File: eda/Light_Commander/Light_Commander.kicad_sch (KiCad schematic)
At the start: 12 parts, among them J1 GATE0, J10 BUFFB, J11 BUFFC, J12 BUFFD, J2 GATE1, J3 GATE2, J4 GATE3, J5 INA, J6 INB, J7 INC, J8 IND, J9 BUFFA

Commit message: Add OLED, LED strip connector, and LED level shifter to schematic
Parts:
- added J15: Conn_01x05, footprints:CUI_TBLH10V-350-05BK, symbol Connector_Generic:Conn_01x05
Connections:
- net GND: now also J15.2 (Pin_2), J15.5 (Pin_5)
- new net +5V_LED: J15.1 (Pin_1), J15.3 (Pin_3)
- new net LED_SPI: J15.4 (Pin_4)

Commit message: Add MDI in and thru to schematic
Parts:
- added J16: MIDI_IN, footprints:PJ301M-12_STEREO, symbol Connector_Audio:AudioJack2_Ground
- added J17: MIDI_THRU, footprints:PJ301M-12_STEREO, symbol Connector_Audio:AudioJack2_Ground
- added SW3, SW4: SW_DPDT_x2, footprints:CAS-220TA, symbol Switch:SW_DPDT_x2
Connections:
- net GND: now also J16.G, J17.G
- new net: J16.T, SW3.3 (C), SW3.4 (A)
- new net: J16.S, SW3.1 (A), SW3.6 (C)
- new net MIDI_IN_PIN_4: SW3.2 (B)
- new net MIDI_IN_PIN_5: SW3.5 (B)
- new net MIDI_THRU_PIN_4: SW4.2 (B)
- new net MIDI_THRU_PIN_5: SW4.5 (B)
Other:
- note added: "TRS MIDI A: Switch up as shown TRS MIDI B: Flipped down"

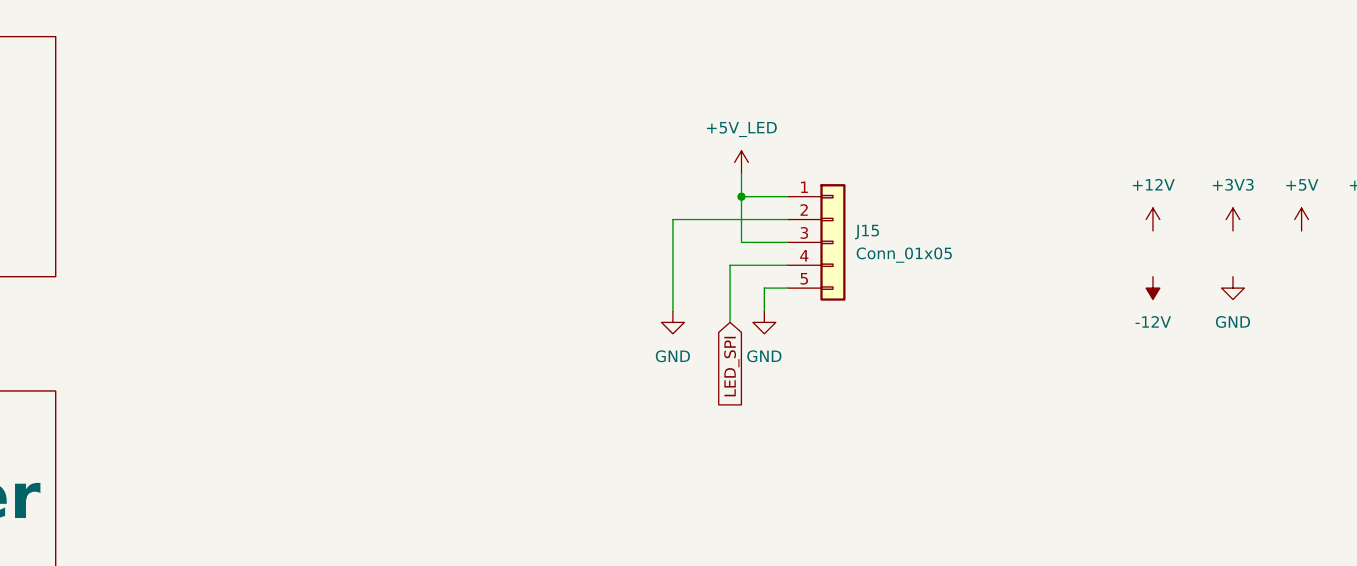
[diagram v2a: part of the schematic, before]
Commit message: Add buttons, SWD, and LED reverse polarity protection to schematic
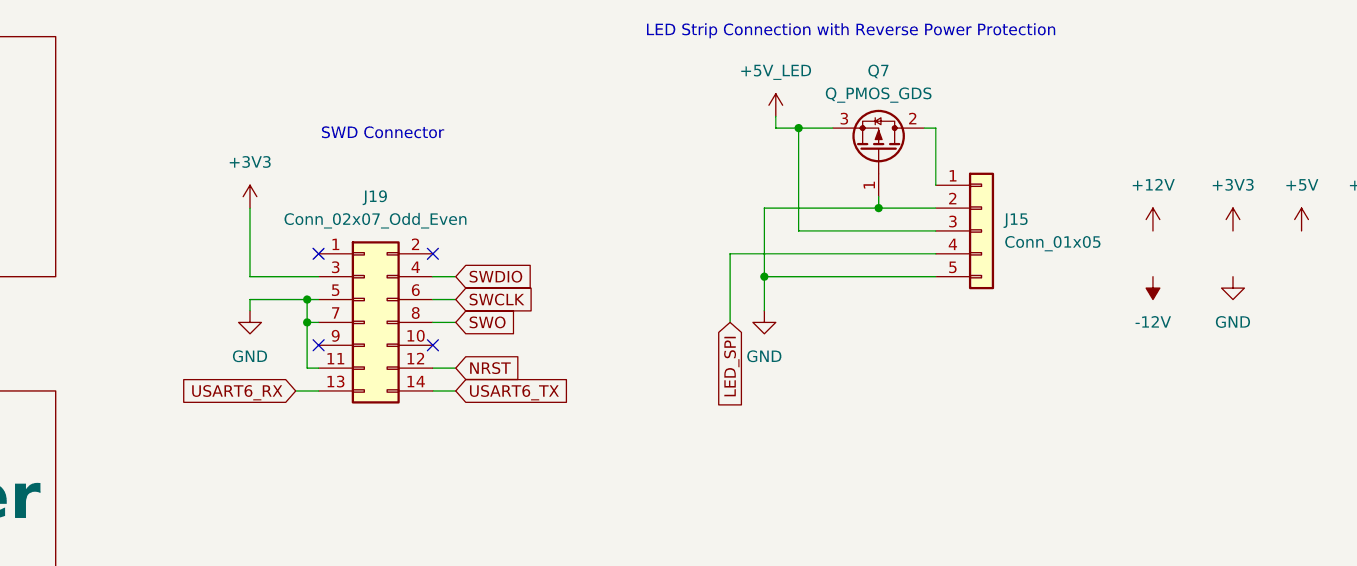
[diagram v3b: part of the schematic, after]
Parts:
- added J19: Conn_02x07_Odd_Even, symbol Connector_Generic:Conn_02x07_Odd_Even
- added Q7: Q_PMOS_GDS, Package_TO_SOT_SMD:TO-252-2, symbol Transistor_FET:Q_PMOS_GDS
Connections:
- net +3V3: now also J19.3 (Pin_3)
- net +5V_LED: now also Q7.3 (S); no longer J15.1 (Pin_1)
- net GND: now also J19.11 (Pin_11), J19.5 (Pin_5), J19.7 (Pin_7), Q7.1 (G)
- new net: J15.1 (Pin_1), Q7.2 (D)
- new net NRST: J19.12 (Pin_12)
- new net SWCLK: J19.6 (Pin_6)
- new net SWDIO: J19.4 (Pin_4)
- new net SWO: J19.8 (Pin_8)
- new net USART6_RX: J19.13 (Pin_13)
- new net USART6_TX: J19.14 (Pin_14)
- no-connect marks 4 -> 8
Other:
- note added: "LED Strip Connection with Reverse Power Protection"
- note added: "SWD Connector"
- moved on the sheet: J15

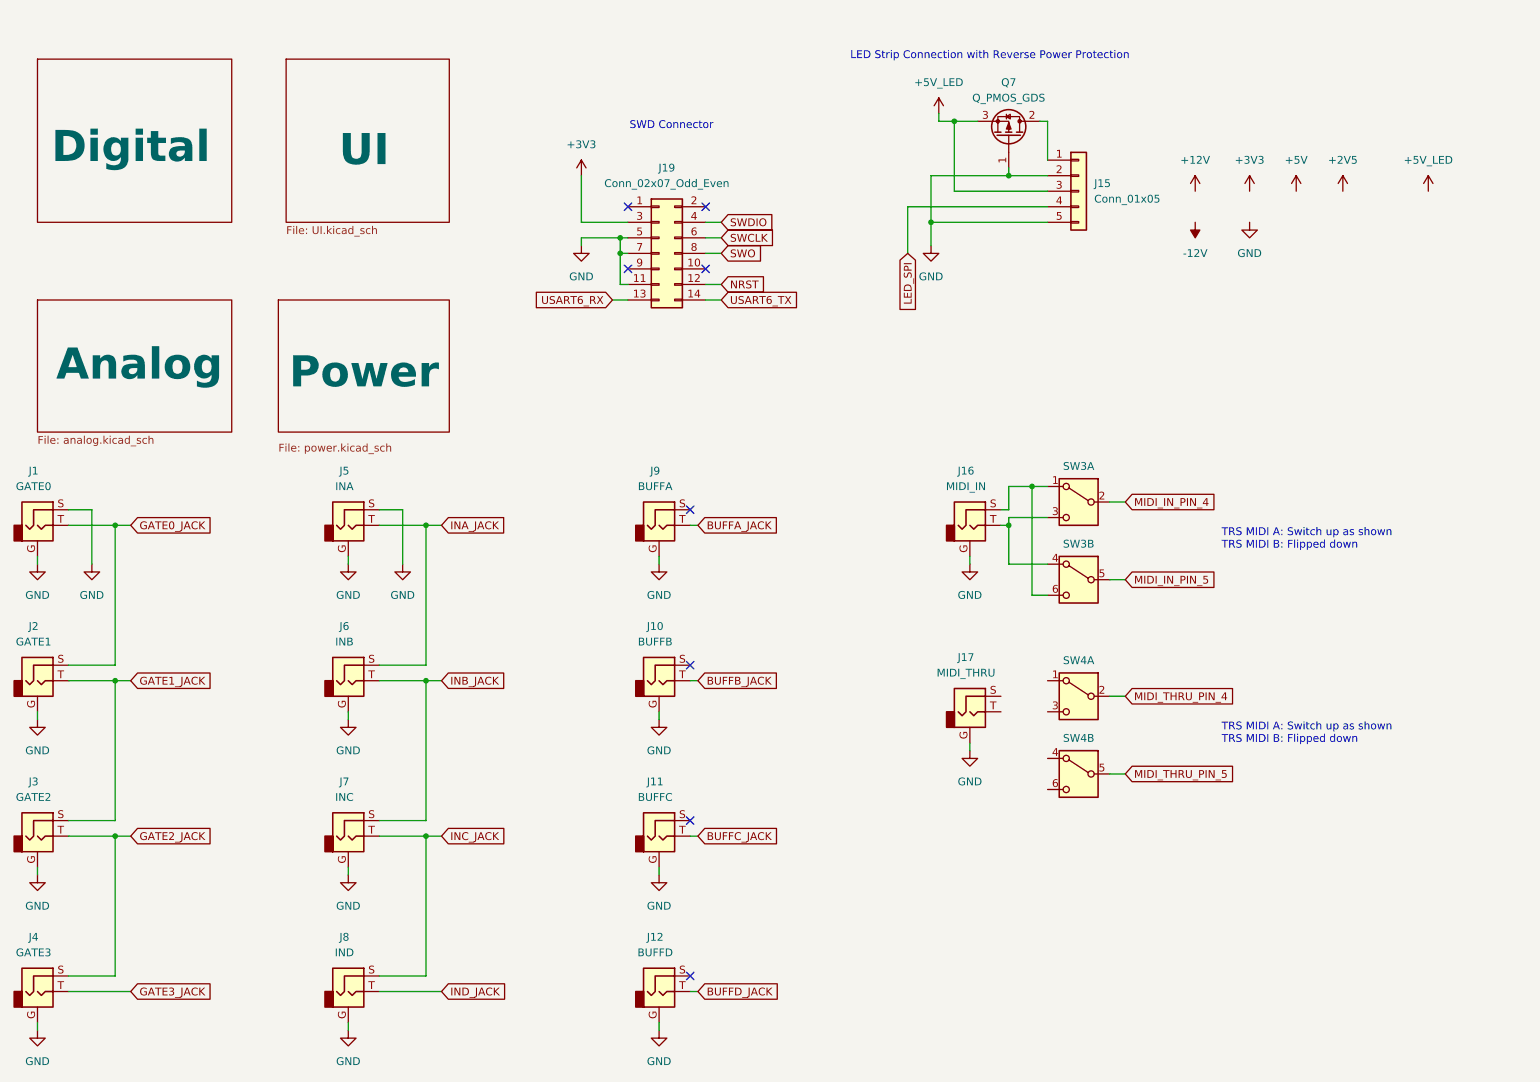
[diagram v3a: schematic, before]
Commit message: Fix footprints and finish first draft of schematic
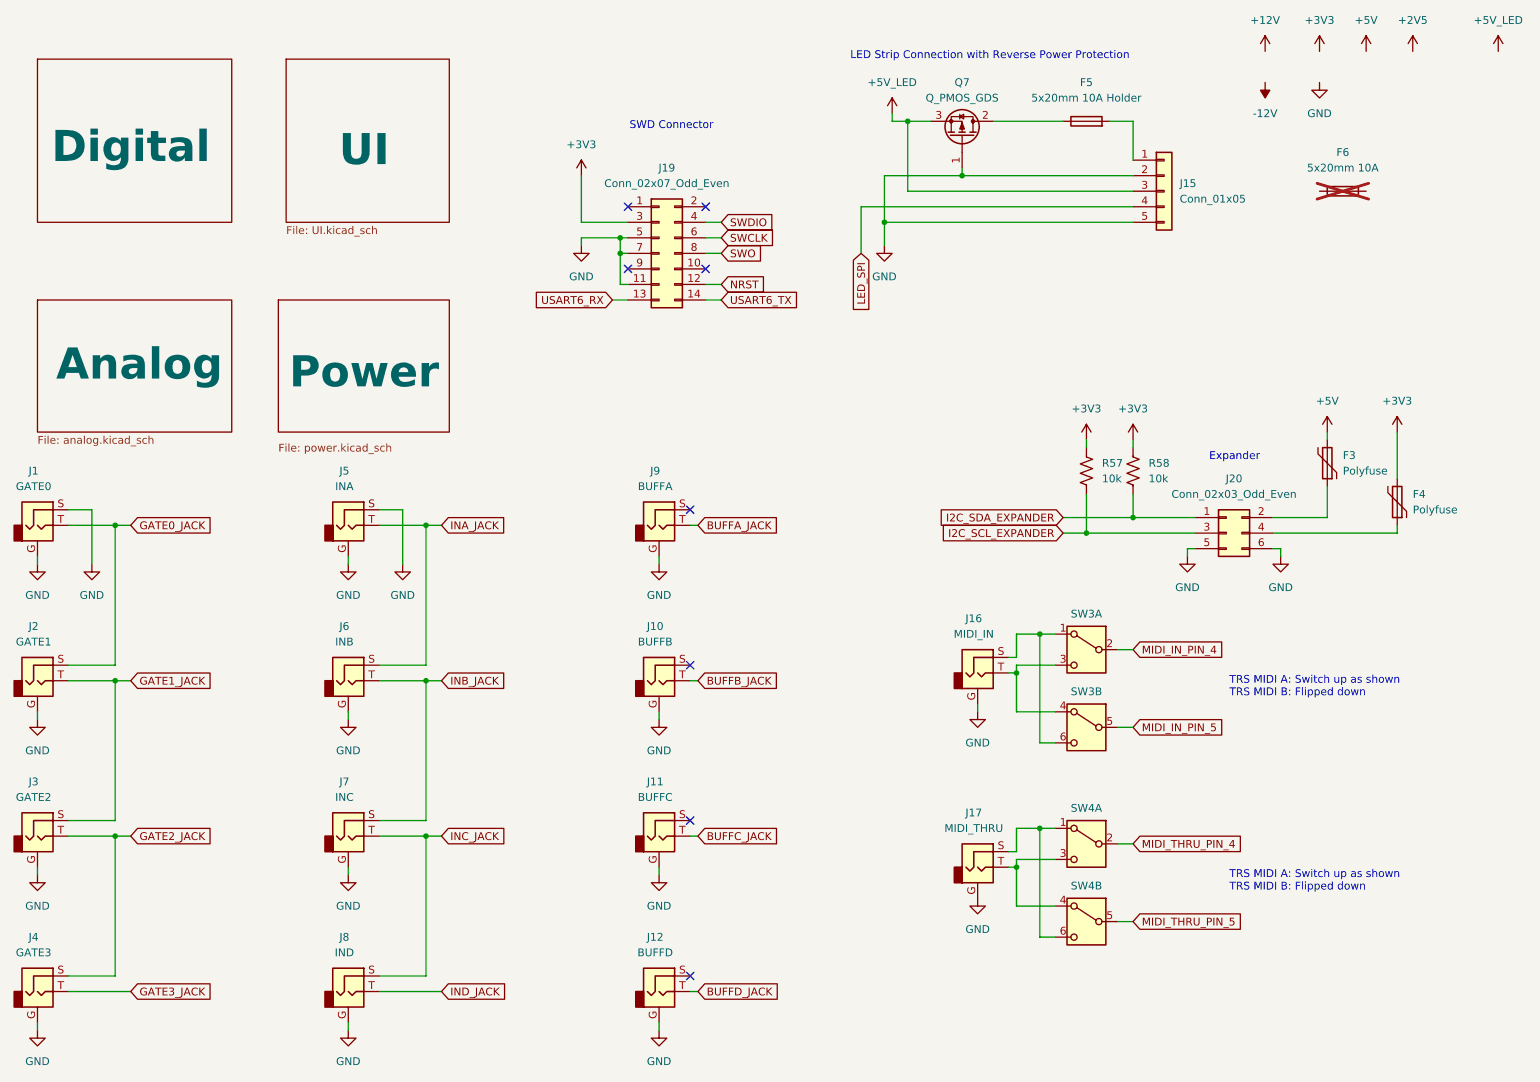
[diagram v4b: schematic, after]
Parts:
- added F3, F4: Polyfuse, Fuse:Fuse_0805_2012Metric, symbol Device:Polyfuse
- added F5: 5x20mm 10A Holder, footprints:05200101Z, symbol Device:Fuse
- added F6: 5x20mm 10A, symbol Device:Fuse
- added J20: Conn_02x03_Odd_Even, Connector_IDC:IDC-Header_2x03_P2.54mm_Vertical, symbol Connector_Generic:Conn_02x03_Odd_Even
- added R57, R58: 10k, Resistor_SMD:R_0805_2012Metric, symbol Device:R_US
- J19: footprint (none) -> footprints:SAMTEC_FTSH-107-01-L-DV-K-A; Digikey_PN (none) -> FTSH-107-01-L-DV-K-A-ND
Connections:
- net +3V3: now also F4.2, R57.1, R58.1
- net +5V: now also F3.2
- net GND: now also J20.5 (Pin_5), J20.6 (Pin_6)
- net at J15.1 (Pin_1): now also F5.2; no longer Q7.2 (D)
- net at SW4.4 (A): now also J17.T, SW4.3 (C)
- net at SW4.6 (C): now also J17.S, SW4.1 (A)
- new net: F4.1, J20.4 (Pin_4)
- new net: F5.1, Q7.2 (D)
- new net: F3.1, J20.2 (Pin_2)
- new net I2C_SCL_EXPANDER: J20.3 (Pin_3), R57.2
- new net I2C_SDA_EXPANDER: J20.1 (Pin_1), R58.2
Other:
- note added: "Expander"
- moved on the sheet: J15, J16, J17, Q7, SW3A, SW3B, SW4A, SW4B

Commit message: Start of PCB
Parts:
- added N1: Housing, footprints:Light_Commander_Panel, symbol Mechanical:Housing
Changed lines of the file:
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@@
+	)
+	(symbol
+		(lib_id "Mechanical:Housing")
+		(at 163.83 78.74 0)
+		(unit 1)
+		(body_style 1)
+		(exclude_from_sim no)
+		(in_bom no)
+		(on_board yes)
+		(in_pos_files yes)
+		(dnp no)
+		(fields_autoplaced yes)
+		(property "Reference" "N1"
+			(at 167.64 77.7874 0)
+			(show_name no)
+			(do_not_autoplace no)
+			(effects
+				(font
+					(size 1.27 1.27)
+				)
+				(justify left)
+			)
+		)
+		(property "Value" "Housing"
+			(at 167.64 80.3274 0)
+			(show_name no)
+			(do_not_autoplace no)
+			(effects
+				(font
+					(size 1.27 1.27)
+				)
+				(justify left)
+			)
+		)
+		(property "Footprint" "footprints:Light_Commander_Panel"
+			(at 165.1 77.47 0)
+			(hide yes)
+			(show_name no)
+			(do_not_autoplace no)
+			(effects
+				(font
+					(size 1.27 1.27)
+				)
+			)
+		)
+		(property "Datasheet" ""
+			(at 165.1 77.47 0)
+			(hide yes)
+			(show_name no)
+			(do_not_autoplace no)
+			(effects
+				(font
+					(size 1.27 1.27)
+				)
+			)
+		)
+		(property "Description" "Housing"
+			(at 163.83 78.74 0)
+			(hide yes)
+			(show_name no)
+			(do_not_autoplace no)
+			(effects
+				(font
+					(size 1.27 1.27)
+				)
+			)
+		)
+		(instances
+			(project "Light_Commander"
+				(path "/dc725142-0bfd-4f8d-931f-2d32b87c7a54"
+					(reference "N1")
+					(unit 1)
+				)
+			)
+		)
 	)
 	(symbol
